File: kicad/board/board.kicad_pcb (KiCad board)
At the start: 2 copper layers, 126.9 x 103.7 mm, 39 parts

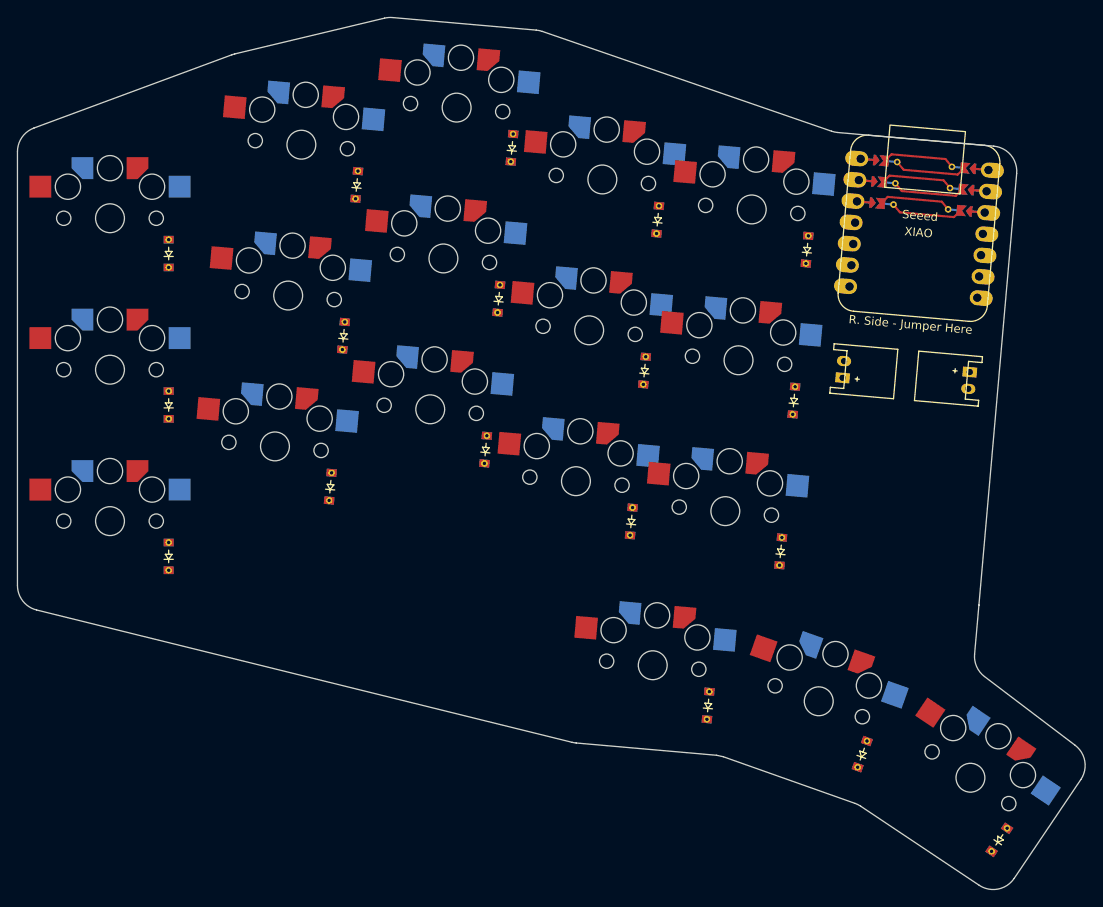
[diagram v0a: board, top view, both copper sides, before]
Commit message: Complete Schematic and Work on PCB Tracings
Schematic should be complete, and most tracings are completed as well. Still some tracings left and design check still needs to be done.
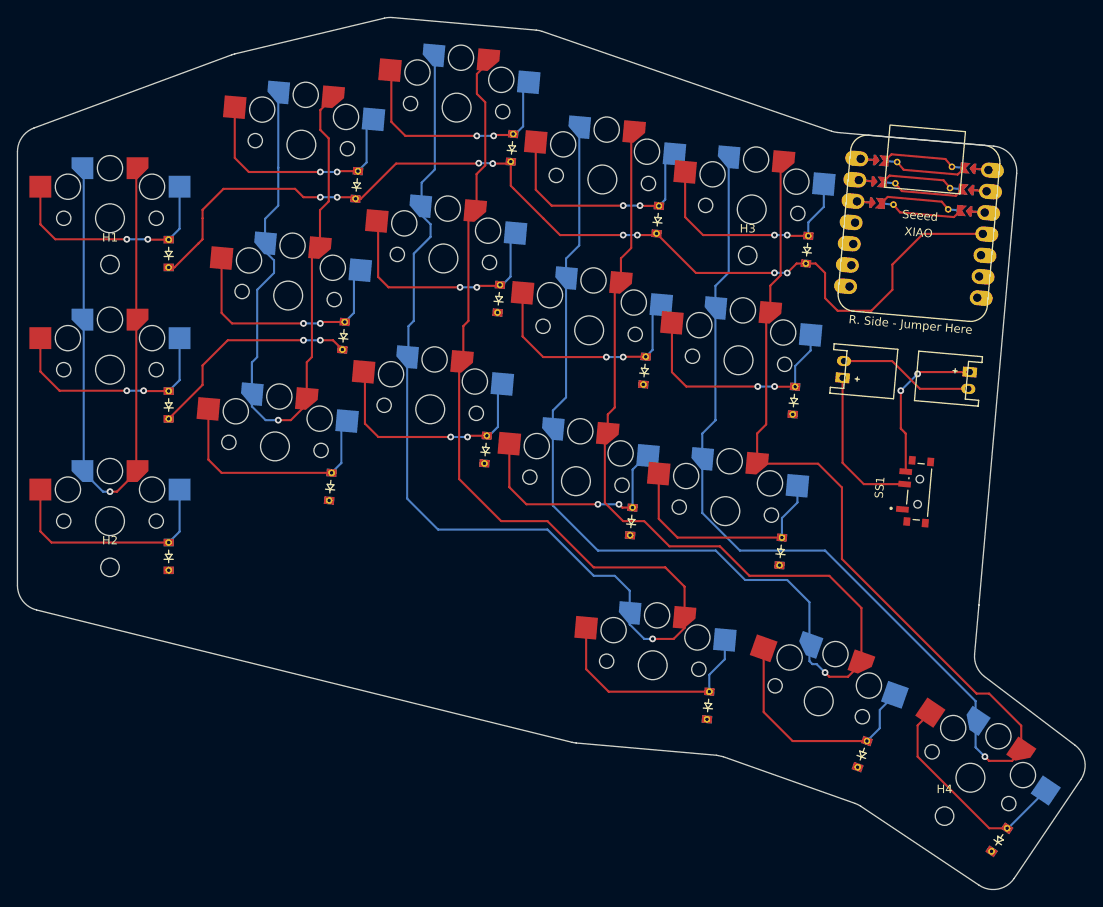
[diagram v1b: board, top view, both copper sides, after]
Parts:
- added H1: MountingHole_2.2mm_M2, MountingHole:MountingHole_2.2mm_M2, F.Cu at (0.00, -30.5)
- added H2: MountingHole_2.2mm_M2, MountingHole:MountingHole_2.2mm_M2, F.Cu at (0.00, 5.50)
- added H3: MountingHole_2.2mm_M2, MountingHole:MountingHole_2.2mm_M2, F.Cu at (75.8, -31.6)
- added H4: MountingHole_2.2mm_M2, MountingHole:MountingHole_2.2mm_M2, F.Cu at (99.2, 35.1)
- added SS1: SW_SSSS811101, clacken:SW_SSSS811101, F.Cu at (96.1, -3.49)
- D1, D10, D11, D12, D13, D14, D15, D16, D17, D18, D2, D3, D4, D5, D6, D7, D8, D9: value 1N914 -> 1N4001
- S1, S10, S11, S12, S13, S14, S15, S16, S17, S18, S2, S3, S4, S5, S6, S7, S8, S9: value SW_Push_45deg -> SW_SPST
- U1: value (none) -> ~
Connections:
- D1 pad 1: Row3 -> R2
- D10 pad 1: Row3 -> R2
- D11 pad 1: Row2 -> R1
- D12 pad 1: Row1 -> R0
- D13 pad 1: Row3 -> R2
- D14 pad 1: Row2 -> R1
- D15 pad 1: Row1 -> R0
- D16 pad 1: Row4 -> R3
- D17 pad 1: Row4 -> R3
- D18 pad 1: Row4 -> R3
- D2 pad 1: Row2 -> R1
- D3 pad 1: Row1 -> R0
- D4 pad 1: Row3 -> R2
- D5 pad 1: Row2 -> R1
- D6 pad 1: Row1 -> R0
- D7 pad 1: Row3 -> R2
- D8 pad 1: Row2 -> R1
- D9 pad 1: Row1 -> R0
- JST2 pad 1: Net-(JST1-Pin_1) -> Net-(JST2-Pin_1)
- S1 pad 1: Col1 -> C0
- S10 pad 1: Col4 -> C3
- S11 pad 1: Col4 -> C3
- S12 pad 1: Col4 -> C3
- S13 pad 1: Col5 -> C4
- S14 pad 1: Col5 -> C4
- S15 pad 1: Col5 -> C4
- S16 pad 1: Col3 -> C2
- S17 pad 1: Col4 -> C3
- S18 pad 1: Col5 -> C4
- S2 pad 1: Col1 -> C0
- S3 pad 1: Col1 -> C0
- S4 pad 1: Col2 -> C1
- S5 pad 1: Col2 -> C1
- S6 pad 1: Col2 -> C1
- S7 pad 1: Col3 -> C2
- S8 pad 1: Col3 -> C2
- S9 pad 1: Col3 -> C2
- U1 pad 0: P0 -> C0
- U1 pad 1: P1 -> C1
- U1 pad 10: P10 -> R0
- U1 pad 11: _1_11 -> unconnected-(U1-V3-Pad11)_4
- U1 pad 12: _1_12 -> unconnected-(U1-GND-Pad12)_3
- U1 pad 13: _1_13 -> unconnected-(U1-VCC-Pad13)_5
- U1 pad 2: P2 -> C2
- U1 pad 3: P3 -> C3
- U1 pad 4: P4 -> C4
- U1 pad 5: P5 -> unconnected-(U1-P5-Pad5)
- U1 pad 6: P6 -> unconnected-(U1-P6-Pad6)
- U1 pad 7: P7 -> R3
- U1 pad 8: P8 -> R2
- U1 pad 9: P9 -> R1
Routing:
- net C2: track 0.00 -> 198.7 mm, vias 0 -> 1
- net C4: track 0.00 -> 186.9 mm, vias 0 -> 1
- net C3: track 0.00 -> 183.9 mm, vias 0 -> 1
- net R0: track 0.00 -> 122.2 mm, vias 0 -> 8
- net C1: track 0.00 -> 100.4 mm, vias 0 -> 1
- net C0: track 0.00 -> 95.4 mm, vias 0 -> 1
- net Net-(D5-A): track 0.00 -> 28.7 mm, vias 0 -> 2
- net Net-(D4-A): track 0.00 -> 28.4 mm
- net Net-(D6-A): track 0.00 -> 28.3 mm, vias 0 -> 2
- net Net-(D17-A): track 0.00 -> 28.2 mm
- net Net-(D14-A): track 0.00 -> 28.1 mm, vias 0 -> 2
- net Net-(D12-A): track 0.00 -> 28.0 mm, vias 0 -> 2
- net Net-(D15-A): track 0.00 -> 27.9 mm, vias 0 -> 2
- net Net-(D13-A): track 0.00 -> 27.9 mm
- net Net-(D10-A): track 0.00 -> 27.9 mm, vias 0 -> 2
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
